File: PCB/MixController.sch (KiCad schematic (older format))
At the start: 11 parts

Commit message: Change to AC/DC converter from USB wall wort
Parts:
- added J? (x2): Conn_01x02, symbol Conn_01x02
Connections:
- net labels added: LINE, NEUT
- wire segments 76 -> 82
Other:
- note added: "+5V"
- note added: "AC/DC Converter"
- note added: "GND"
- note added: "LINE"
- note added: "NEUT"
- note removed: "Panel Mount USB"
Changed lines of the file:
@@
 LIBS:valves
 LIBS:particle
+LIBS:MixController-cache
 EELAYER 25 0
 EELAYER END
@@
 Wire Notes Line
 	3750 6150 4500 6150
-Wire Notes Line
-	4200 1650 5150 1650
-Wire Notes Line
-	5150 1650 5150 2350
-Wire Notes Line
-	5150 2350 4200 2350
-Wire Notes Line
-	4200 2350 4200 1650
-Text Notes 4250 1750 0    60   ~ 0
-Panel Mount USB
-Wire Notes Line
-	5750 3450 5750 2050
-Wire Notes Line
-	5750 2050 5150 2050
-Wire Notes Line
-	5850 3450 5850 1950
-Wire Notes Line
-	5850 1950 5150 1950
 Text Label 7100 3750 0    60   ~ 0
 black
@@
 Text Notes 9500 4950 0    60   ~ 0
 To Motor A
+$Comp
+L Conn_01x02 J?
+U 1 1 5AE82FD7
+P 2150 2350
+F 0 "J?" H 2150 2450 50  0000 C CNN
+F 1 "Conn_01x02" H 2150 2150 50  0001 C CNN
+F 2 "" H 2150 2350 50  0001 C CNN
+F 3 "" H 2150 2350 50  0001 C CNN
+	1    2150 2350
+	1    0    0    -1
+$EndComp
+$Comp
+L Conn_01x02 J?
+U 1 1 5AE8311E
+P 2750 2450
+F 0 "J?" H 2750 2550 50  0000 C CNN
+F 1 "Conn_01x02" H 2750 2250 50  0001 C CNN
+F 2 "" H 2750 2450 50  0001 C CNN
+F 3 "" H 2750 2450 50  0001 C CNN
+	1    2750 2450
+	-1   0    0    1
+$EndComp
+Text Notes 2200 2400 0    60   ~ 0
+LINE
+Text Notes 2200 2500 0    60   ~ 0
+NEUT
+Text Notes 2700 2400 2    60   ~ 0
++5V
+Text Notes 2700 2500 2    60   ~ 0
+GND
+Wire Notes Line
+	2000 2150 2000 2600
+Wire Notes Line
+	2000 2600 2900 2600
+Wire Notes Line
+	2900 2600 2900 2150
+Wire Notes Line
+	2900 2150 2000 2150
+Text Notes 2100 2100 0    60   ~ 0
+AC/DC Converter
+Wire Wire Line
+	1950 2350 1550 2350
+Wire Wire Line
+	1950 2450 1550 2450
+Wire Wire Line
+	2950 2350 3150 2350
+Wire Wire Line
+	3150 2350 3150 2150
+Wire Wire Line
+	2950 2450 3150 2450
+Wire Wire Line
+	3150 2450 3150 2700
+$Comp
+L +5V #PWR?
+U 1 1 5AE8362F
+P 3150 2150
+F 0 "#PWR?" H 3150 2000 50  0001 C CNN
+F 1 "+5V" H 3150 2290 50  0000 C CNN
+F 2 "" H 3150 2150 50  0001 C CNN
+F 3 "" H 3150 2150 50  0001 C CNN
+	1    3150 2150
+	1    0    0    -1
+$EndComp
+$Comp
+L GND #PWR?
+U 1 1 5AE83748
+P 3150 2700
+F 0 "#PWR?" H 3150 2450 50  0001 C CNN
+F 1 "GND" H 3150 2550 50  0000 C CNN
+F 2 "" H 3150 2700 50  0001 C CNN
+F 3 "" H 3150 2700 50  0001 C CNN
+	1    3150 2700
+	1    0    0    -1
+$EndComp
+Text Label 1550 2350 0    60   ~ 0
+LINE
+Text Label 1550 2450 0    60   ~ 0
+NEUT
 $EndSCHEMATC

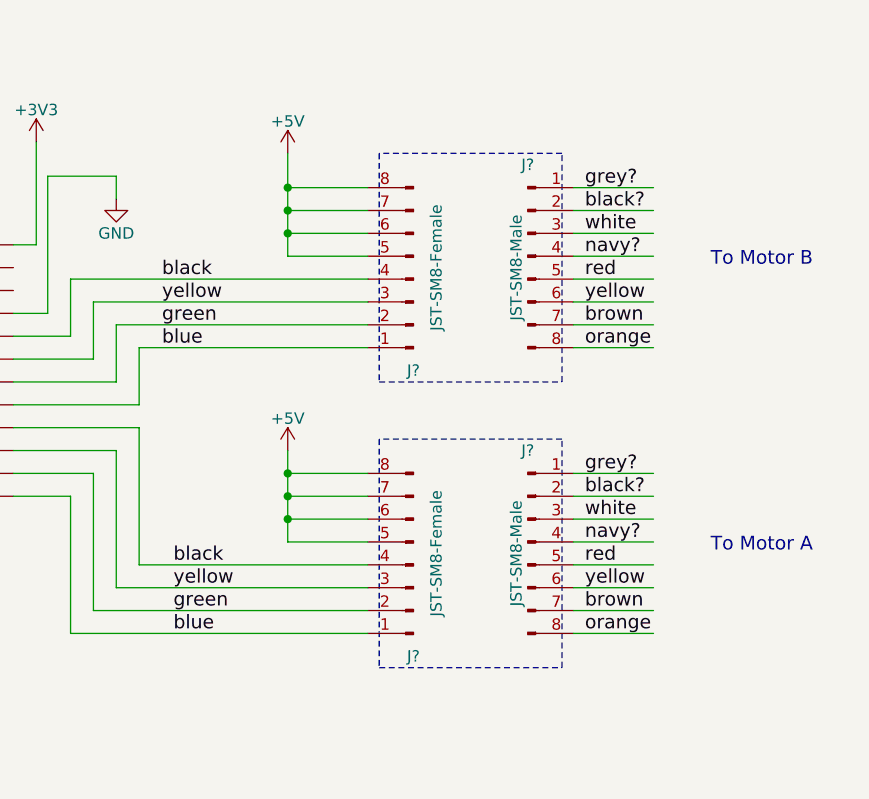
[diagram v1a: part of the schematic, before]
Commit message: Fix wire colors
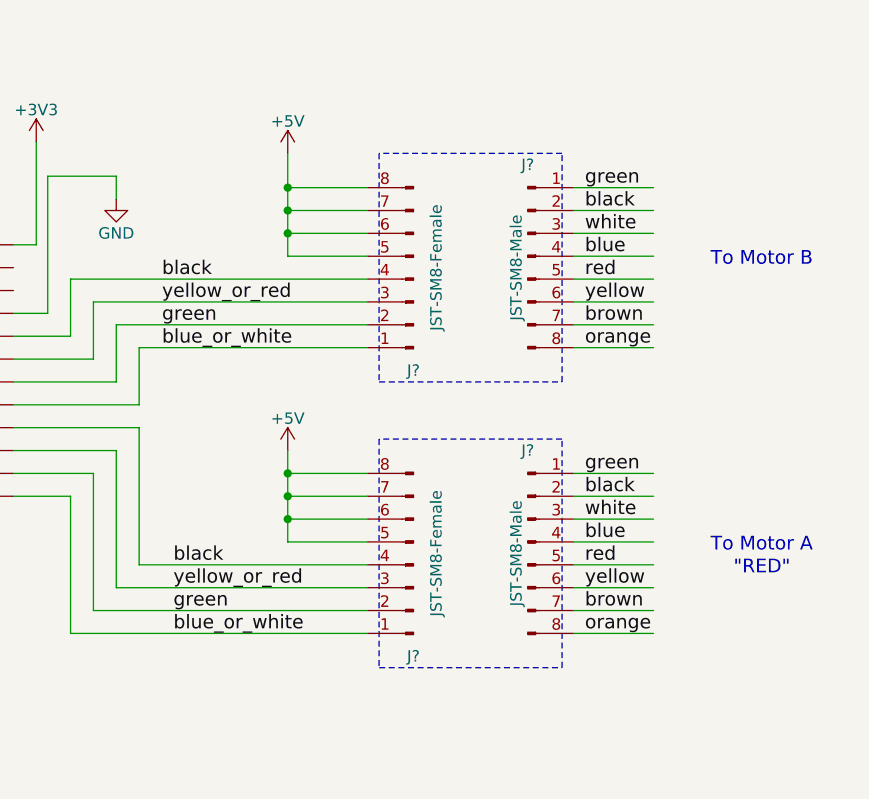
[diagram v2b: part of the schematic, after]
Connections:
- net labels added: blue_or_white, yellow_or_red
- net labels removed: black?, grey?, navy?
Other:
- note added: ""RED""
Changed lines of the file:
@@
 Wire Wire Line
 	8900 5000 9250 5000
-Wire Wire Line
-	8900 4900 9250 4900
-Wire Wire Line
-	8900 4800 9250 4800
-Wire Wire Line
-	8900 4700 9250 4700
-Wire Wire Line
-	8900 4600 9250 4600
-Text Label 8950 4800 0    60   ~ 0
-white
-Text Label 8950 4600 0    60   ~ 0
-grey?
-Text Label 8950 4700 0    60   ~ 0
-black?
-Text Label 8950 4900 0    60   ~ 0
-navy?
 Text Label 8950 5000 0    60   ~ 0
 red
@@
 white
 Text Label 8950 3350 0    60   ~ 0
-grey?
+green
 Text Label 8950 3450 0    60   ~ 0
-black?
+black
 Text Label 8950 3650 0    60   ~ 0
-navy?
+blue
 Text Label 8950 3750 0    60   ~ 0
 red
@@
 Text Label 7100 3750 0    60   ~ 0
 black
-Text Label 7100 3850 0    60   ~ 0
-yellow
 Text Label 7100 3950 0    60   ~ 0
 green
-Text Label 7100 4050 0    60   ~ 0
-blue
 Text Label 7150 5000 0    60   ~ 0
 black
 Text Label 7150 5100 0    60   ~ 0
-yellow
+yellow_or_red
 Text Label 7150 5200 0    60   ~ 0
 green
 Text Label 7150 5300 0    60   ~ 0
-blue
+blue_or_white
 Text Notes 800  1200 0    60   ~ 0
 NOTES:\nButton uses 3.3V source while motors use 5V source\nWire colors on motor side are best guess based on photos\nYou may want to use a 9 or 10 pin connector for Motor B to prevent them from being plugged incorrectly\nJST SM connectors picked for panel mount, swap with any connector available
@@
 Text Label 1550 2450 0    60   ~ 0
 NEUT
+Wire Wire Line
+	8900 4900 9250 4900
+Wire Wire Line
+	8900 4800 9250 4800
+Wire Wire Line
+	8900 4700 9250 4700
+Wire Wire Line
+	8900 4600 9250 4600
+Text Label 8950 4800 0    60   ~ 0
+white
+Text Label 8950 4600 0    60   ~ 0
+green
+Text Label 8950 4700 0    60   ~ 0
+black
+Text Label 8950 4900 0    60   ~ 0
+blue
+Text Notes 9600 5050 0    60   ~ 0
+"RED"
+Text Label 7100 4050 0    60   ~ 0
+blue_or_white
+Text Label 7100 3850 0    60   ~ 0
+yellow_or_red
 $EndSCHEMATC

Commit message: save all stashed
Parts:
- added J? (x2): Conn_01x02, symbol Conn_01x02
- added K?: Relay, Relays_THT:Relay_SPDT_SANYOU_SRD_Series_Form_A, symbol SANYOU_SRD_Form_A
- added SW?: SW_Push, symbol SW_Push
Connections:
- net labels added: +48V
- net labels removed: LINE, NEUT
- wire segments 82 -> 98
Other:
- note added: "DC/DC Converter \n(36-72V to 5V @1000mA)"
- note added: "MOTOR A POWER"
- note added: "MOTOR B POWER"
- note added: "VIN+"
- note added: "VIN-"
- note removed: "AC/DC Converter"
- note removed: "LINE"
- note removed: "NEUT"
- moved on the sheet: J?
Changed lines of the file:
@@
 Text Label 7150 5300 0    60   ~ 0
 blue_or_white
-Text Notes 800  1200 0    60   ~ 0
+Text Notes 5950 6300 0    60   ~ 0
 NOTES:\nButton uses 3.3V source while motors use 5V source\nWire colors on motor side are best guess based on photos\nYou may want to use a 9 or 10 pin connector for Motor B to prevent them from being plugged incorrectly\nJST SM connectors picked for panel mount, swap with any connector available
 Text Notes 9500 3700 0    60   ~ 0
@@
 L Conn_01x02 J?
 U 1 1 5AE82FD7
-P 2150 2350
-F 0 "J?" H 2150 2450 50  0000 C CNN
-F 1 "Conn_01x02" H 2150 2150 50  0001 C CNN
-F 2 "" H 2150 2350 50  0001 C CNN
-F 3 "" H 2150 2350 50  0001 C CNN
-	1    2150 2350
+P 3150 1100
+F 0 "J?" H 3150 1200 50  0000 C CNN
+F 1 "Conn_01x02" H 3150 900 50  0001 C CNN
+F 2 "" H 3150 1100 50  0001 C CNN
+F 3 "" H 3150 1100 50  0001 C CNN
+	1    3150 1100
 	1    0    0    -1
 $EndComp
@@
 L Conn_01x02 J?
 U 1 1 5AE8311E
-P 2750 2450
-F 0 "J?" H 2750 2550 50  0000 C CNN
-F 1 "Conn_01x02" H 2750 2250 50  0001 C CNN
-F 2 "" H 2750 2450 50  0001 C CNN
-F 3 "" H 2750 2450 50  0001 C CNN
-	1    2750 2450
+P 3750 1200
+F 0 "J?" H 3750 1300 50  0000 C CNN
+F 1 "Conn_01x02" H 3750 1000 50  0001 C CNN
+F 2 "" H 3750 1200 50  0001 C CNN
+F 3 "" H 3750 1200 50  0001 C CNN
+	1    3750 1200
 	-1   0    0    1
 $EndComp
-Text Notes 2200 2400 0    60   ~ 0
-LINE
-Text Notes 2200 2500 0    60   ~ 0
-NEUT
-Text Notes 2700 2400 2    60   ~ 0
+Text Notes 3200 1150 0    60   ~ 0
+VIN+
+Text Notes 3200 1250 0    60   ~ 0
+VIN-
+Text Notes 3700 1150 2    60   ~ 0
 +5V
-Text Notes 2700 2500 2    60   ~ 0
+Text Notes 3700 1250 2    60   ~ 0
 GND
 Wire Notes Line
-	2000 2150 2000 2600
-Wire Notes Line
-	2000 2600 2900 2600
-Wire Notes Line
-	2900 2600 2900 2150
-Wire Notes Line
-	2900 2150 2000 2150
-Text Notes 2100 2100 0    60   ~ 0
-AC/DC Converter
-Wire Wire Line
-	1950 2350 1550 2350
-Wire Wire Line
-	1950 2450 1550 2450
-Wire Wire Line
-	2950 2350 3150 2350
-Wire Wire Line
-	3150 2350 3150 2150
-Wire Wire Line
-	2950 2450 3150 2450
-Wire Wire Line
-	3150 2450 3150 2700
+	3000 900  3000 1350
+Wire Notes Line
+	3000 1350 3900 1350
+Wire Notes Line
+	3900 1350 3900 900
+Wire Notes Line
+	3900 900  3000 900
+Text Notes 2900 850  0    60   ~ 0
+DC/DC Converter \n(36-72V to 5V @1000mA)
+Wire Wire Line
+	2550 1100 2950 1100
+Wire Wire Line
+	3950 1100 4250 1100
+Wire Wire Line
+	4250 1100 4250 900
+Wire Wire Line
+	3950 1200 4250 1200
+Wire Wire Line
+	4250 1200 4250 1450
 $Comp
 L +5V #PWR?
 U 1 1 5AE8362F
-P 3150 2150
-F 0 "#PWR?" H 3150 2000 50  0001 C CNN
-F 1 "+5V" H 3150 2290 50  0000 C CNN
-F 2 "" H 3150 2150 50  0001 C CNN
-F 3 "" H 3150 2150 50  0001 C CNN
-	1    3150 2150
+P 4250 900
+F 0 "#PWR?" H 4250 750 50  0001 C CNN
+F 1 "+5V" H 4250 1040 50  0000 C CNN
+F 2 "" H 4250 900 50  0001 C CNN
+F 3 "" H 4250 900 50  0001 C CNN
+	1    4250 900
 	1    0    0    -1
 $EndComp
@@
 L GND #PWR?
 U 1 1 5AE83748
-P 3150 2700
-F 0 "#PWR?" H 3150 2450 50  0001 C CNN
-F 1 "GND" H 3150 2550 50  0000 C CNN
-F 2 "" H 3150 2700 50  0001 C CNN
-F 3 "" H 3150 2700 50  0001 C CNN
-	1    3150 2700
-	1    0    0    -1
-$EndComp
-Text Label 1550 2350 0    60   ~ 0
-LINE
-Text Label 1550 2450 0    60   ~ 0
-NEUT
+P 4250 1450
+F 0 "#PWR?" H 4250 1200 50  0001 C CNN
+F 1 "GND" H 4250 1300 50  0000 C CNN
+F 2 "" H 4250 1450 50  0001 C CNN
+F 3 "" H 4250 1450 50  0001 C CNN
+	1    4250 1450
+	1    0    0    -1
+$EndComp
 Wire Wire Line
 	8900 4900 9250 4900
@@
 Text Label 7100 3850 0    60   ~ 0
 yellow_or_red
+$Comp
+L +48V #PWR?
+U 1 1 5B0684B5
+P 1900 800
+F 0 "#PWR?" H 1900 650 50  0001 C CNN
+F 1 "+48V" H 1900 940 50  0000 C CNN
+F 2 "" H 1900 800 50  0001 C CNN
+F 3 "" H 1900 800 50  0001 C CNN
+	1    1900 800
+	1    0    0    -1
+$EndComp
+Wire Wire Line
+	2550 1100 2550 2600
+$Comp
+L SANYOU_SRD_Form_A K?
+U 1 1 5B0686B1
+P 1700 1450
+F 0 "K?" H 2050 1600 50  0000 L CNN
+F 1 "Relay" H 2050 1500 50  0000 L CNN
+F 2 "Relays_THT:Relay_SPDT_SANYOU_SRD_Series_Form_A" H 2950 1400 50  0001 C CNN
+F 3 "" H 1700 1450 50  0001 C CNN
+	1    1700 1450
+	1    0    0    -1
+$EndComp
+$Comp
+L SW_Push SW?
+U 1 1 5B0687B7
+P 1100 2100
+F 0 "SW?" H 1150 2200 50  0000 L CNN
+F 1 "SW_Push" H 1100 2040 50  0001 C CNN
+F 2 "" H 1100 2300 50  0001 C CNN
+F 3 "" H 1100 2300 50  0001 C CNN
+	1    1100 2100
+	1    0    0    -1
+$EndComp
+$Comp
+L GND #PWR?
+U 1 1 5B068C6B
+P 750 2250
+F 0 "#PWR?" H 750 2000 50  0001 C CNN
+F 1 "GND" H 750 2100 50  0000 C CNN
+F 2 "" H 750 2250 50  0001 C CNN
+F 3 "" H 750 2250 50  0001 C CNN
+	1    750  2250
+	1    0    0    -1
+$EndComp
+Wire Wire Line
+	1300 2100 1500 2100
+Wire Wire Line
+	1500 2100 1500 1750
+Wire Wire Line
+	900  2100 750  2100
+Wire Wire Line
+	750  2100 750  2250
+$Comp
+L Conn_01x02 J?
+U 1 1 5B069086
+P 3150 1900
+F 0 "J?" H 3150 2000 50  0000 C CNN
+F 1 "Conn_01x02" H 3150 1700 50  0000 C CNN
+F 2 "" H 3150 1900 50  0001 C CNN
+F 3 "" H 3150 1900 50  0001 C CNN
+	1    3150 1900
+	1    0    0    -1
+$EndComp
+$Comp
+L Conn_01x02 J?
+U 1 1 5B0690C9
+P 3150 2600
+F 0 "J?" H 3150 2700 50  0000 C CNN
+F 1 "Conn_01x02" H 3150 2400 50  0000 C CNN
+F 2 "" H 3150 2600 50  0001 C CNN
+F 3 "" H 3150 2600 50  0001 C CNN
+	1    3150 2600
+	1    0    0    -1
+$EndComp
+$Comp
+L GND #PWR?
+U 1 1 5B069148
+P 2800 2850
+F 0 "#PWR?" H 2800 2600 50  0001 C CNN
+F 1 "GND" H 2800 2700 50  0000 C CNN
+F 2 "" H 2800 2850 50  0001 C CNN
+F 3 "" H 2800 2850 50  0001 C CNN
+	1    2800 2850
+	1    0    0    -1
+$EndComp
+Wire Wire Line
+	2950 2700 2800 2700
+Wire Wire Line
+	2800 2700 2800 2850
+$Comp
+L GND #PWR?
+U 1 1 5B069209
+P 2800 2150
+F 0 "#PWR?" H 2800 1900 50  0001 C CNN
+F 1 "GND" H 2800 2000 50  0000 C CNN
+F 2 "" H 2800 2150 50  0001 C CNN
+F 3 "" H 2800 2150 50  0001 C CNN
+	1    2800 2150
+	1    0    0    -1
+$EndComp
+Wire Wire Line
+	2950 2000 2800 2000
+Wire Wire Line
+	2800 2000 2800 2150
+Wire Wire Line
+	1900 800  1900 1150
+Wire Wire Line
+	1900 950  1500 950
+Wire Wire Line
+	1500 950  1500 1150
+Connection ~ 1900 950
+Wire Wire Line
+	2950 1200 2800 1200
+Wire Wire Line
+	2800 1200 2800 1450
+Wire Wire Line
+	1900 1900 2950 1900
+Wire Wire Line
+	2550 2600 2950 2600
+Connection ~ 2550 1900
+$Comp
+L GND #PWR?
+U 1 1 5B069C92
+P 2800 1450
+F 0 "#PWR?" H 2800 1200 50  0001 C CNN
+F 1 "GND" H 2800 1300 50  0000 C CNN
+F 2 "" H 2800 1450 50  0001 C CNN
+F 3 "" H 2800 1450 50  0001 C CNN
+	1    2800 1450
+	1    0    0    -1
+$EndComp
+Text Notes 3250 2000 0    60   ~ 0
+MOTOR B POWER
+Text Notes 3250 2700 0    60   ~ 0
+MOTOR A POWER
+Wire Wire Line
+	1900 1750 1900 1900
 $EndSCHEMATC

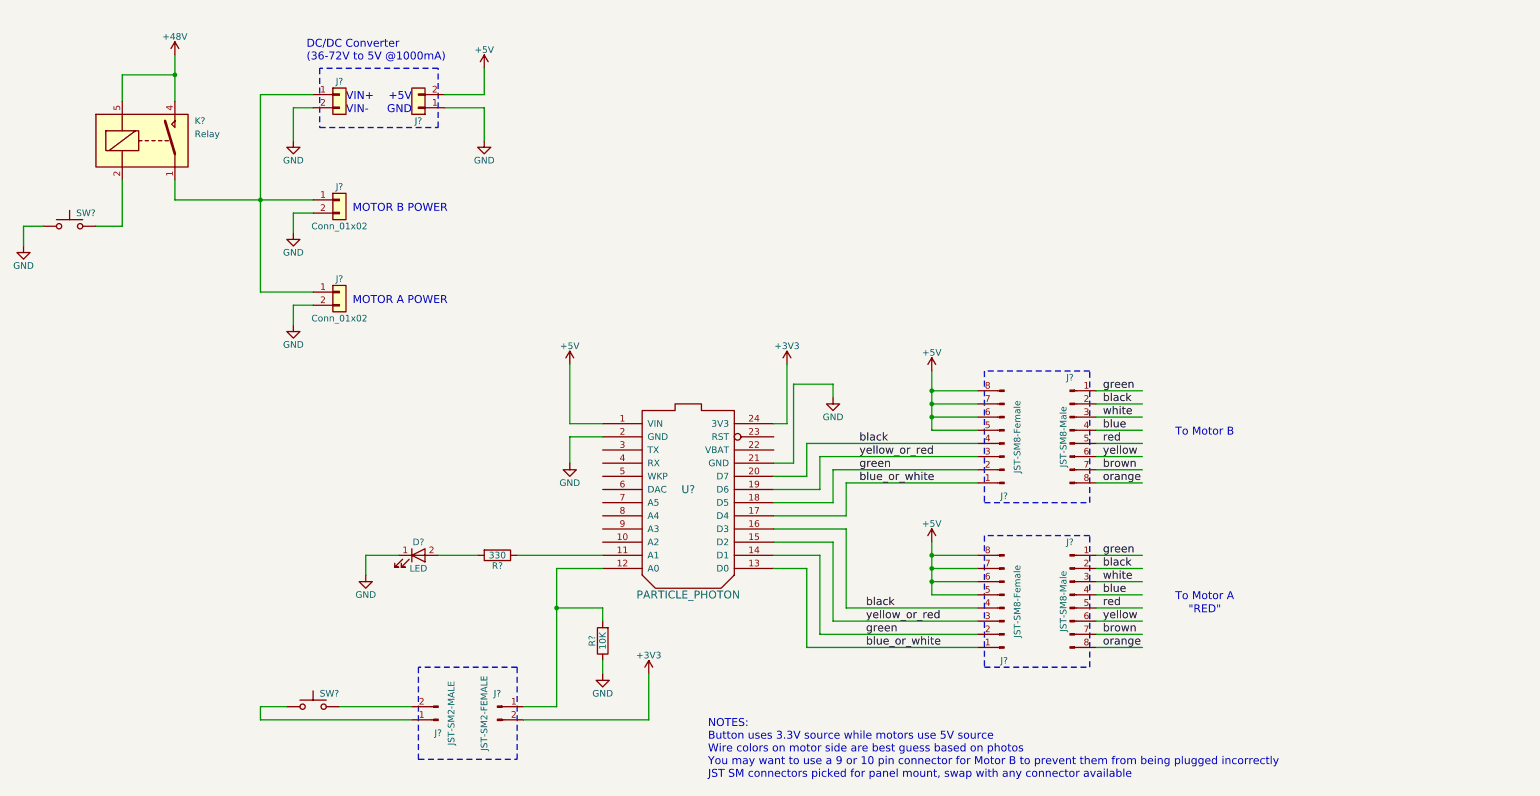
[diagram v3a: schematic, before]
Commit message: Add Radio and Level Translator
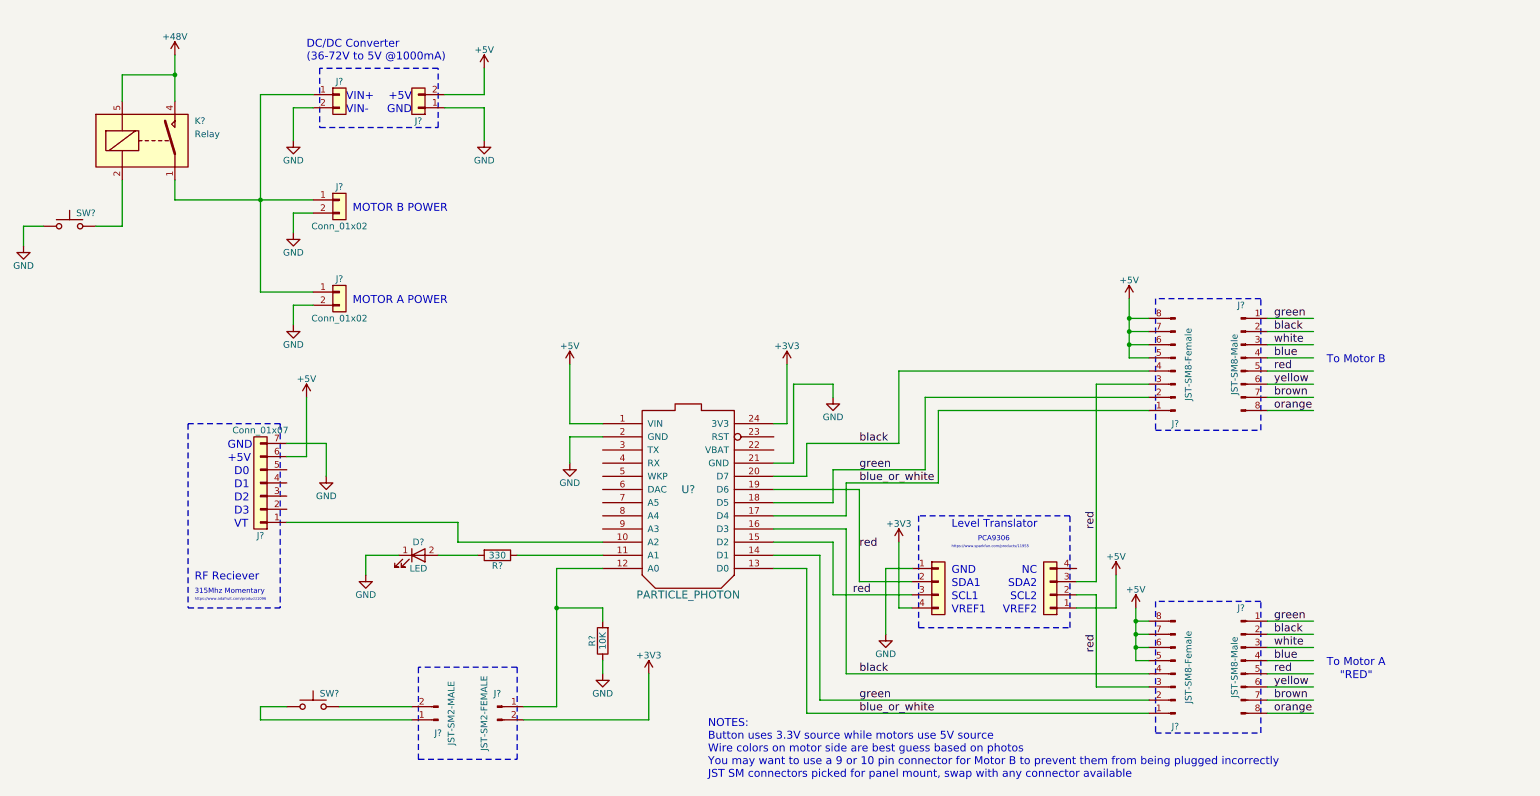
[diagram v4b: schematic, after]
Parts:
- added J?: Conn_01x07, symbol Conn_01x07
- added J? (x2): Conn_01x04, symbol Conn_01x04
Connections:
- net labels removed: yellow_or_red
- wire segments 98 -> 123
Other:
- note added: "315Mhz Momentary"
- note added: "D0"
- note added: "D1"
- note added: "D2"
- note added: "D3"
- note added: "Level Translator"
- note added: "NC"
- note added: "PCA9306"
- note added: "RF Reciever"
- note added: "SCL1"
- note added: "SCL2"
- note added: "SDA1"
- note added: "SDA2"
- note added: "VREF1"
- note added: "VREF2"
- note added: "VT"
- note added: "https://www.adafruit.com/product/1096"
- note added: "https://www.sparkfun.com/products/11955"
- moved on the sheet: J?
